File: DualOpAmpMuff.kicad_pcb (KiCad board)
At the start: 4 copper layers, 97 parts, among them J101 IO, Q101 2N7002, Q102 2N7002, SW101 SW_SPDT, SW102 SW_SPDT, U101 LM324, U102 RC4558

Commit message: switched to 2 layer
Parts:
- added J102: ScopeGroundLoop, Connector:THT_GND_WIRE, B.Cu at (43.5, -47.6)
- added TP101: GN_A, TestPoint:TestPoint_THTPad_D2.0mm_Drill1.0mm_VAL, B.Cu at (13.8, -7.65)
- added TP102: FLT_A, TestPoint:TestPoint_THTPad_D2.0mm_Drill1.0mm_VAL, B.Cu at (23.1, -48.9)
- added TP103: R_A, TestPoint:TestPoint_THTPad_D2.0mm_Drill1.0mm_VAL, B.Cu at (58.4, -53.4)
- added TP104: B1, TestPoint:TestPoint_THTPad_D2.0mm_Drill1.0mm_VAL, B.Cu at (8.35, -6.05)
- added TP105: B2, TestPoint:TestPoint_THTPad_D2.0mm_Drill1.0mm_VAL, B.Cu at (55.6, -15.8)
- added TP106: VG_A, TestPoint:TestPoint_THTPad_D2.0mm_Drill1.0mm_VAL, B.Cu at (73.3, -15.2)
- added TP107: IN_A, TestPoint:TestPoint_THTPad_D2.0mm_Drill1.0mm_VAL, B.Cu at (29.1, -5.05)
- added TP108: OUT_A, TestPoint:TestPoint_THTPad_D2.0mm_Drill1.0mm_VAL, B.Cu at (66.6, -52.6)
- added TP109: GN_B, TestPoint:TestPoint_THTPad_D2.0mm_Drill1.0mm_VAL, B.Cu at (17.8, -5.45)
- added TP110: VG_B, TestPoint:TestPoint_THTPad_D2.0mm_Drill1.0mm_VAL, B.Cu at (46.3, -9.40)
- added TP111: FLT_B, TestPoint:TestPoint_THTPad_D2.0mm_Drill1.0mm_VAL, B.Cu at (34.5, -37.9)
- added TP112: IN_B, TestPoint:TestPoint_THTPad_D2.0mm_Drill1.0mm_VAL, B.Cu at (41.0, -13.1)
- added TP113: R_B, TestPoint:TestPoint_THTPad_D2.0mm_Drill1.0mm_VAL, B.Cu at (51.1, -30.1)
- added TP114: OUT_B, TestPoint:TestPoint_THTPad_D2.0mm_Drill1.0mm_VAL, B.Cu at (68.3, -28.9)
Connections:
- net /COM_A renamed /FULL_A
- net /COM_B renamed /FULL_B
- net Net-(C108-Pad2) renamed /FLT_A
- net Net-(C119-Pad2) renamed /FLT_B
- net Net-(D102-K) renamed /VGND_A
- net Net-(D108-K) renamed /VGND_B
- net Net-(R107-Pad2) renamed /Gain_A
- net Net-(R121-Pad2) renamed /Gain_B
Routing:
- net FX_OUT_A: track 2.70 -> 78.7 mm
- net Net-(SW101-A): track 0.00 -> 59.2 mm
- net /RAW_A: track 14.2 -> 70.6 mm, vias 0 -> 1
- net /Gain_B: track 8.05 -> 24.7 mm
- net /FLT_B: track 14.7 -> 21.2 mm
- net FX_OUT_B: track 58.0 -> 52.0 mm
- net /LP_A: track 0.00 -> 4.44 mm
- net /HP_A: track 0.00 -> 4.42 mm
- net /Bias2: track 21.6 -> 26.0 mm
- net /FLT_A: track 36.6 -> 41.0 mm
- net FX_IN_B: track 8.65 -> 12.6 mm
- net /Bias1: track 32.8 -> 36.6 mm
- net GND: track 27.2 -> 29.9 mm, vias 21 -> 23
- net Net-(C116-Pad2): track 0.00 -> 2.74 mm
- net /Gain_A: track 12.9 -> 15.2 mm
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- added copper zone on B.Cu, net GND
- added copper zone on F.Cu, net GND
- removed copper zone on In1.Cu, net GND
- removed copper zone on In2.Cu, net GND
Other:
- copper layers 4 -> 2

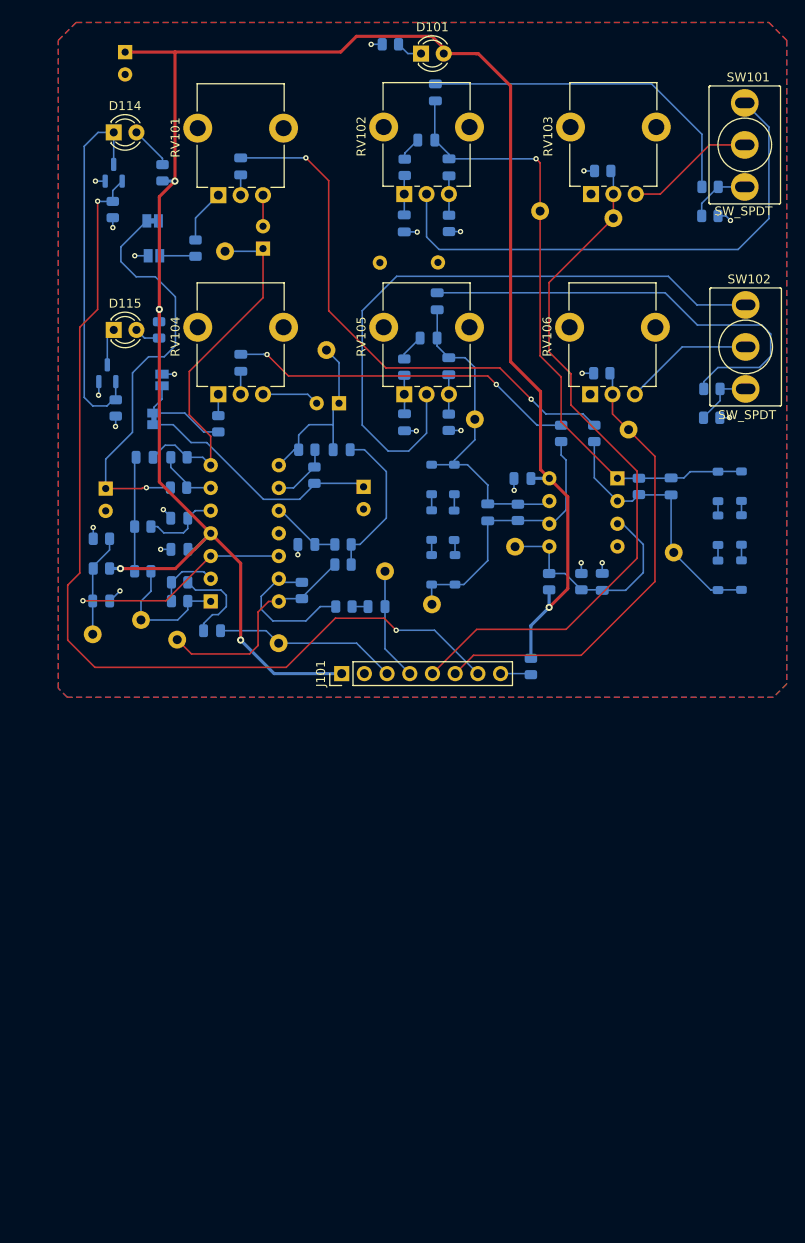
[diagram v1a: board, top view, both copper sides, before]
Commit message: smaller outline laid out
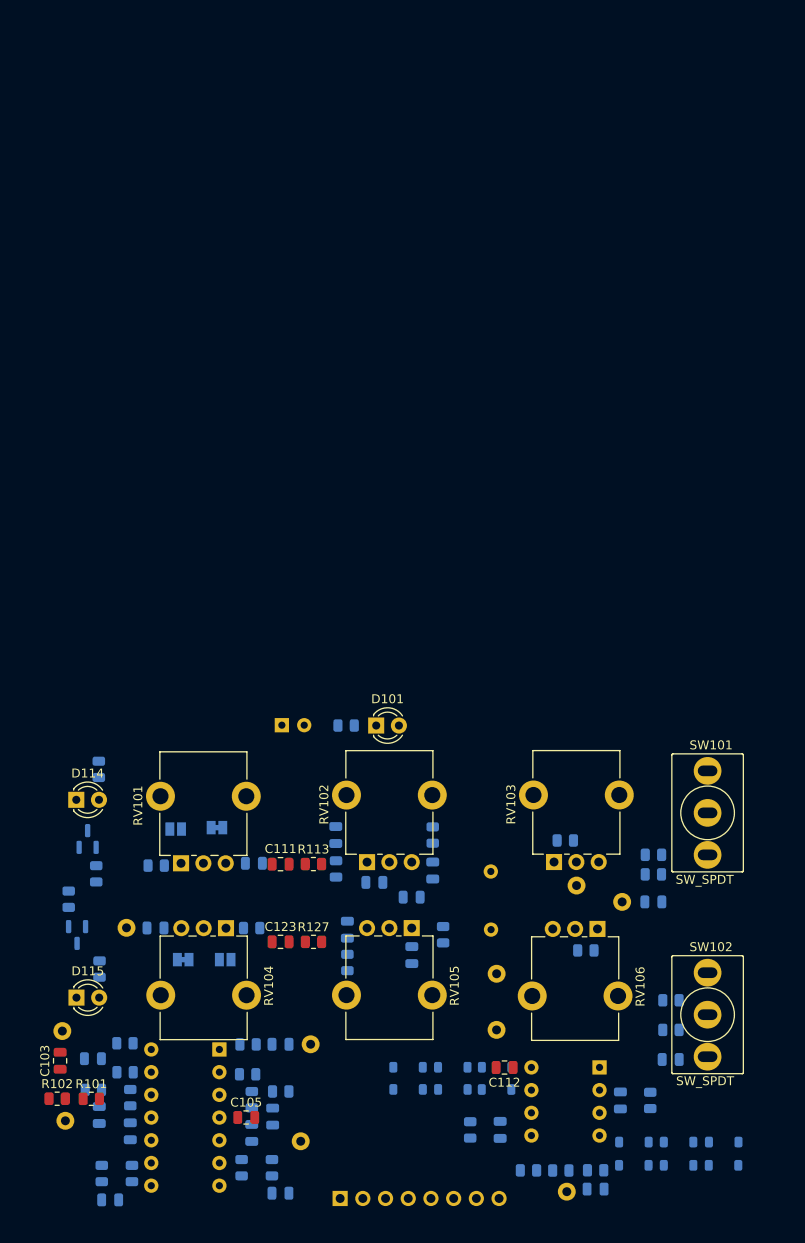
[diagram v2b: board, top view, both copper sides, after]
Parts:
- removed C122: 10u, Capacitor_THT:CP_Radial_D5.0mm_P2.50mm
- removed TP101: GN_A, TestPoint:TestPoint_THTPad_D2.0mm_Drill1.0mm_VAL
- removed TP106: VG_A, TestPoint:TestPoint_THTPad_D2.0mm_Drill1.0mm_VAL
- removed TP109: GN_B, TestPoint:TestPoint_THTPad_D2.0mm_Drill1.0mm_VAL
- removed TP110: VG_B, TestPoint:TestPoint_THTPad_D2.0mm_Drill1.0mm_VAL
- added C102: 10u, Capacitor_SMD:C_0805_2012Metric, B.Cu at (29.4, 56.5)
- C103, C105, C111, C112, C123, R101, R102, R113, R127: moved to F.Cu
- C109, C110, C121: footprint Capacitor_THT:CP_Radial_D5.0mm_P2.50mm -> Capacitor_SMD:C_0805_2012Metric
- J101: moved to B.Cu
- moved C110 107.8 mm to (10.3, 57.2), turned to 0 degrees
- moved TP102 99.9 mm to (31.6, 50.7), turned to -90 degrees
- moved C115 93.8 mm to (71.1, 23.9), turned to 0 degrees
- moved C126 88.8 mm to (73.0, 41.5), turned to 0 degrees
- moved R125 83.3 mm to (12.7, 54.3), turned to -90 degrees
- moved C116 83.3 mm to (39.9, 21.7)
- moved R124 81.7 mm to (9.36, 54.3)
- moved R110 79.8 mm to (25.0, 53.6), turned to -90 degrees
- moved C119 79.2 mm to (9.08, 47.7), turned to -90 degrees
- moved R116 78.9 mm to (35.6, 20.2), turned to 90 degrees
- moved C114 78.7 mm to (46.4, 20.4), turned to 90 degrees
- moved C111 78.2 mm to (29.4, 19.7), turned to 0 degrees
- moved TP103 77.8 mm to (67.6, 23.9)
- moved C101 77.3 mm to (29.5, 4.12), turned to 0 degrees
- moved R117 77.2 mm to (71.1, 20.8)
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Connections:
- C109 pad 1: Net-(JP102-A) -> Net-(C109-Pad1)
- C109 pad 2: GND -> /FLT_A
- C110 pad 1: /FLT_A -> Net-(JP103-A)
- C110 pad 2: Net-(C110-Pad2) -> GND
- C121 pad 1: Net-(JP103-A) -> /FLT_B
- C121 pad 2: GND -> Net-(C121-Pad2)
- RV101 pad 3: Net-(C110-Pad2) -> Net-(C109-Pad1)
- RV104 pad 3: Net-(C122-Pad2) -> Net-(C121-Pad2)
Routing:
- net +9V: track 221.1 -> 0.00 mm, vias 5 -> 0
- net SW_MID: track 107.2 -> 0.00 mm, vias 2 -> 0
- net FX_OUT_A: track 78.7 -> 0.00 mm
- net Net-(SW102-A): track 72.2 -> 0.00 mm
- net /RAW_A: track 70.6 -> 0.00 mm, vias 1 -> 0
- net Net-(C111-Pad2): track 60.5 -> 0.00 mm, vias 2 -> 0
- net Net-(SW101-A): track 59.2 -> 0.00 mm
- net FX_OUT_B: track 52.0 -> 0.00 mm
- net Net-(C126-Pad2): track 51.2 -> 0.00 mm
- net Net-(JP102-A): track 46.5 -> 0.00 mm, vias 1 -> 0
- net Net-(D114-K): track 41.9 -> 0.00 mm
- net /FLT_A: track 41.0 -> 0.00 mm
- net Net-(C123-Pad2): track 39.1 -> 0.00 mm, vias 2 -> 0
- net Net-(C115-Pad2): track 38.0 -> 0.00 mm
- net /RAW_B: track 37.5 -> 0.00 mm
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- removed copper zone on B.Cu, net GND
- removed copper zone on F.Cu, net GND
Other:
- copper layers 2 -> 4

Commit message: preliminary routing
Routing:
- net +9V: track 0.00 -> 176.4 mm, vias 0 -> 4
- net SW_MID: track 0.00 -> 94.3 mm
- net /RAW_A: track 0.00 -> 74.4 mm
- net /RAW_B: track 0.00 -> 73.6 mm, vias 0 -> 1
- net FX_IN_B: track 0.00 -> 64.9 mm
- net /FLT_B: track 0.00 -> 63.1 mm
- net /VGND_A: track 0.00 -> 58.7 mm, vias 0 -> 1
- net /FLT_A: track 0.00 -> 54.4 mm
- net Net-(JP102-A): track 0.00 -> 53.3 mm
- net FX_OUT_A: track 0.00 -> 48.2 mm
- net Net-(SW101-A): track 0.00 -> 45.4 mm
- net Net-(SW102-A): track 0.00 -> 43.2 mm, vias 0 -> 1
- net /VGND_B: track 0.00 -> 40.4 mm, vias 0 -> 1
- net FX_OUT_B: track 0.00 -> 39.8 mm
- net GND: track 0.00 -> 36.9 mm, vias 0 -> 22
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- added copper zone on In1.Cu, net GND
- added copper zone on In2.Cu, net GND

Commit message: DRC passing on 2 layer
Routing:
- net FX_IN_B: track 64.9 -> 80.0 mm, vias 0 -> 2
- net +9V: track 176.4 -> 177.3 mm, vias 4 -> 3
- added copper zone on B.Cu, net GND
- added copper zone on F.Cu, net GND
- removed copper zone on In1.Cu, net GND
- removed copper zone on In2.Cu, net GND
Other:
- board outline added: 82 x 60 mm
- copper layers 4 -> 2
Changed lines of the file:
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@@
 	(layers
 		(0 "F.Cu" signal)
-		(1 "In1.Cu" signal)
-		(2 "In2.Cu" signal)
 		(31 "B.Cu" signal)
 		(32 "B.Adhes" user "B.Adhesive")
@@
 			)
 			(layer "dielectric 1"
-				(type "prepreg")
-				(thickness 0.1)
-				(material "FR4")
-				(epsilon_r 4.5)
-				(loss_tangent 0.02)
-			)
-			(layer "In1.Cu"
-				(type "copper")
-				(thickness 0.035)
-			)
-			(layer "dielectric 2"
 				(type "core")
-				(thickness 1.24)
-				(material "FR4")
-				(epsilon_r 4.5)
-				(loss_tangent 0.02)
-			)
-			(layer "In2.Cu"
-				(type "copper")
-				(thickness 0.035)
-			)
-			(layer "dielectric 3"
-				(type "prepreg")
-				(thickness 0.1)
+				(thickness 1.51)
 				(material "FR4")
 				(epsilon_r 4.5)
@@
 		(tags "SOT TO_SOT_SMD")
 		(property "Reference" "Q102"
-			(at 0 2.4 90)
+			(at 0.007501 2.65 90)
 			(layer "B.SilkS")
 			(effects
@@
 		(tags "SOT TO_SOT_SMD")
 		(property "Reference" "Q101"
-			(at 0 2.4 90)
+			(at 0 2.72 90)
 			(layer "B.SilkS")
 			(effects
@@
 		)
 	)
-	(gr_rect
-		(start 0 -0.025)
-		(end 82 75.975)
-		(locked yes)
+	(gr_line
+		(start 79 0)
+		(end 82 3)
 		(stroke
-			(width 0.1)
+			(width 0.05)
 			(type default)
 		)
-		(fill none)
-		(layer "User.3")
+		(layer "Edge.Cuts")
+	)
+	(gr_line
+		(start 0 57.5)
+		(end 0 3)
+		(stroke
+			(width 0.05)
+			(type default)
+		)
+		(layer "Edge.Cuts")
+	)
+	(gr_line
+		(start 79 60)
+		(end 2.5 60)
+		(stroke
+			(width 0.05)
+			(type default)
+		)
+		(layer "Edge.Cuts")
+	)
+	(gr_line
+		(start 3 0)
+		(end 79 0)
+		(stroke
+			(width 0.05)
+			(type default)
+		)
+		(layer "Edge.Cuts")
+	)
+	(gr_line
+		(start 2.5 60)
+		(end 0 57.5)
+		(stroke
+			(width 0.05)
+			(type default)
+		)
+		(layer "Edge.Cuts")
+	)
+	(gr_line
+		(start 82 3)
+		(end 82 57)
+		(stroke
+			(width 0.05)
+			(type default)
+		)
+		(layer "Edge.Cuts")
+	)
+	(gr_line
+		(start 82 57)
+		(end 79 60)
+		(stroke
+			(width 0.05)
+			(type default)
+		)
+		(layer "Edge.Cuts")
+	)
+	(gr_line
+		(start 0 3)
+		(end 3 0)
+		(stroke
+			(width 0.05)
+			(type default)
+		)
+		(layer "Edge.Cuts")
 	)
 	(gr_line
@@
 	)
 	(segment
-		(start 57.43 42.41)
-		(end 56.261006 42.41)
-		(width 0.35)
-		(layer "F.Cu")
-		(net 6)
-	)
-	(segment
 		(start 12.75 35.35)
 		(end 15.85 38.45)
@@
 	)
 	(segment
+		(start 57.42 42.42)
+		(end 57.43 42.41)
+		(width 0.35)
+		(layer "F.Cu")
+		(net 6)
+	)
+	(segment
 		(start 36.030001 51.9)
 		(end 36.030001 57.07)
@@
 	)
 	(segment
+		(start 55.369999 42.42)
+		(end 57.42 42.42)
+		(width 0.35)
+		(layer "F.Cu")
+		(net 6)
+	)
+	(segment
 		(start 42.605 4.16)
 		(end 39.265 7.5)
@@
 	)
 	(segment
-		(start 56.261006 42.41)
-		(end 56.24 42.388994)
-		(width 0.35)
-		(layer "F.Cu")
-		(net 6)
-	)
-	(segment
 		(start 36.030001 49.130001)
 		(end 36.030001 51.9)
@@
 	)
 	(via
-		(at 56.24 42.388994)
-		(size 0.8)
-		(drill 0.4)
-		(layers "F.Cu" "B.Cu")
-		(net 6)
-	)
-	(via
 		(at 11.83875 5.33875)
 		(size 0.8)
@@
 	)
 	(segment
+		(start 30 57.75)
+		(end 20.7 57.75)
+		(width 0.17)
+		(layer "F.Cu")
+		(net 18)
+	)
+	(segment
 		(start 3.01 38.34)
 		(end 4.95 38.34)
@@
 	)
 	(segment
-		(start 34.6 58.85)
-		(end 33.5 57.75)
+		(start 32.45 55.8)
+		(end 30.5 57.75)
 		(width 0.17)
 		(layer "F.Cu")
@@
 	)
 	(segment
-		(start 41.870001 58.85)
-		(end 34.6 58.85)
+		(start 43.650001 57.07)
+		(end 43.650001 50.200001)
 		(width 0.17)
 		(layer "F.Cu")
@@
 	)
 	(segment
-		(start 43.650001 57.07)
-		(end 41.870001 58.85)
+		(start 30.5 57.75)
+		(end 30 57.75)
 		(width 0.17)
 		(layer "F.Cu")
@@
 	)
 	(segment
-		(start 33.5 57.75)
-		(end 20.7 57.75)
+		(start 43.650001 50.200001)
+		(end 43.65 50.2)
 		(width 0.17)
 		(layer "F.Cu")
@@
 		(net 18)
 	)
+	(via
+		(at 32.45 55.8)
+		(size 0.6)
+		(drill 0.3)
+		(layers "F.Cu" "B.Cu")
+		(net 18)
+	)
+	(via
+		(at 43.65 50.2)
+		(size 0.6)
+		(drill 0.3)
+		(layers "F.Cu" "B.Cu")
+		(net 18)
+	)
+	(segment
+		(start 34.65 47.9)
+		(end 34.65 53.6)
+		(width 0.17)
+		(layer "B.Cu")
+		(net 18)
+	)
+	(segment
+		(start 40.15 46.7)
+		(end 35.85 46.7)
+		(width 0.17)
+		(layer "B.Cu")
+		(net 18)
+	)
+	(segment
+		(start 35.85 46.7)
+		(end 34.65 47.9)
+		(width 0.17)
+		(layer "B.Cu")
+		(net 18)
+	)
+	(segment
+		(start 43.65 50.2)
+		(end 40.15 46.7)
+		(width 0.17)
+		(layer "B.Cu")
+		(net 18)
+	)
+	(segment
+		(start 34.65 53.6)
+		(end 32.45 55.8)
+		(width 0.17)
+		(layer "B.Cu")
+		(net 18)
+	)
 	(segment
 		(start 7.420001 41.43)
@@
 		(net 22)
 		(net_name "GND")
-		(layers "In1.Cu" "In2.Cu")
+		(layers "F&B.Cu")
 		(hatch edge 0.5)
+		(priority 1)
 		(connect_pads
-			(clearance 0.2)
+			(clearance 0.25)
 		)
 		(min_thickness 0.25)
@@
 		(polygon
 			(pts
-				(xy 2.5 59.5) (xy 0.5 57.5) (xy 0.5 3.5) (xy 4 0.5) (xy 79 0.5) (xy 81.5 3.5) (xy 81.5 57) (xy 79 59.5)
+				(xy 2.5 59.5) (xy 0.5 57.5) (xy 0.5 3.5) (xy 4 0.5) (xy 79 0.5) (xy 81.5 3) (xy 81.5 57) (xy 79 59.5)
 			)
 		)

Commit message: silkscreen done, routing cleaned up
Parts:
- moved TP103 7.04 mm to (73.3, 28.0), turned to 90 degrees
- moved TP112 0.95 mm to (4.00, 38.3)
- turned TP107 to 0 degrees
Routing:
- net Net-(C123-Pad1): track 8.28 -> 11.1 mm
- net /RAW_A: track 74.4 -> 77.0 mm
- net /Bias2: track 25.6 -> 23.2 mm
- net +9V: track 177.3 -> 176.4 mm
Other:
- board text added: "+9v"
- board text added: "COM"
- board text added: "Dual Muff"
- board text added: "GND"
- board text added: "IN_A"
- board text added: "IN_B"
- board text added: "OUT_A"
- board text added: "OUT_B"
- board text added: "Rev. 5- Dec. 2023 Hayden Setlik"
- board text added: "SW_A"
